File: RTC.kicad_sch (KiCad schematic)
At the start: 14 parts, among them J17 Molex 470531000, U11 EMC2301-1-ACZL-TR, U14 74LVC1G07SE-7, U8 PCF85063AT/AAZ, Y2 X32K768S301

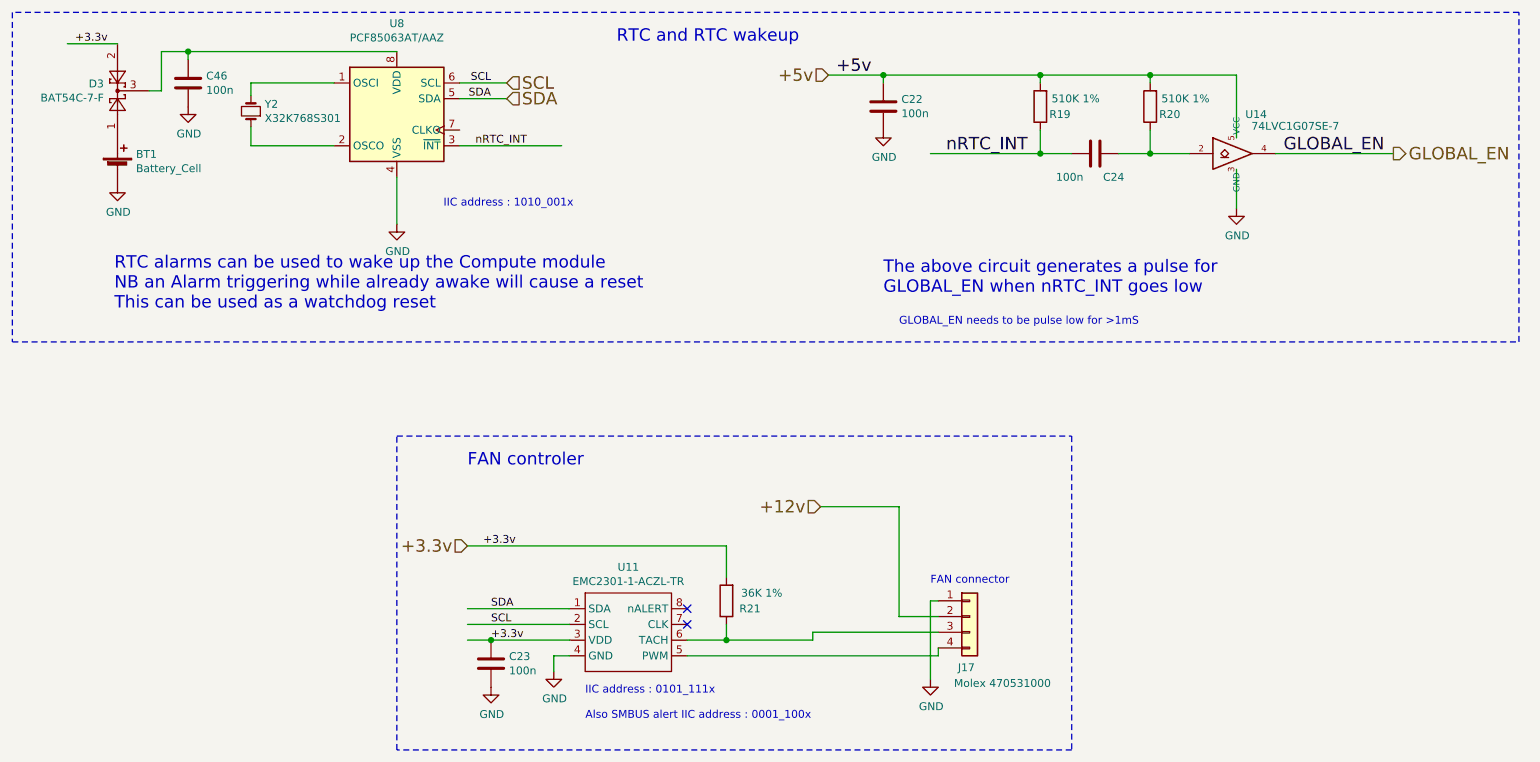
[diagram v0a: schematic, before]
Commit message: Removing unneeded items
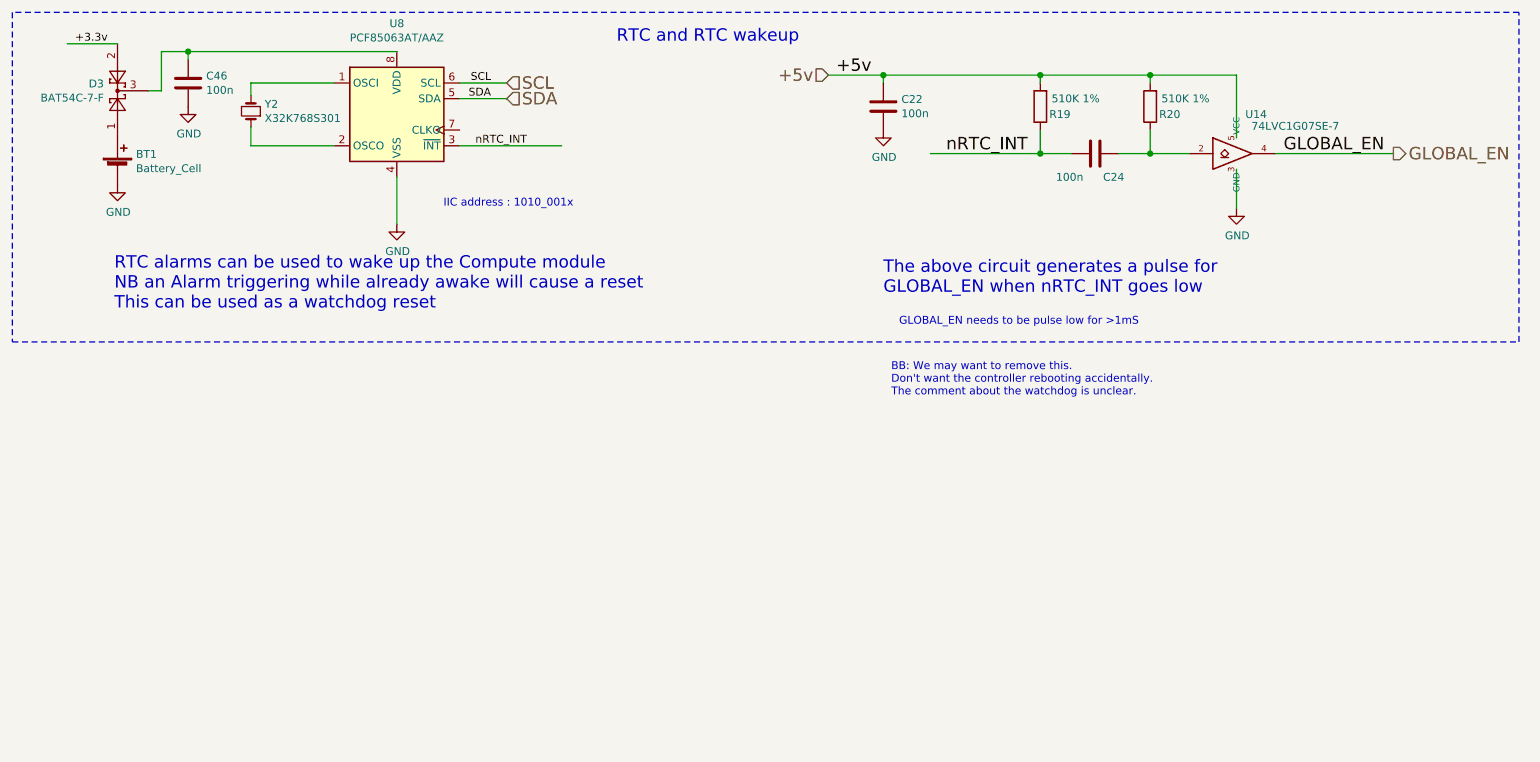
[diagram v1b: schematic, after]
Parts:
- removed C23: 100n, Capacitor_SMD:C_0402_1005Metric, symbol Device:C
- removed J17: Molex 470531000, Connector:FanPinHeader_1x04_P2.54mm_Vertical, symbol Connector_Generic:Conn_01x04
- removed R21: 36K 1%, Resistor_SMD:R_0402_1005Metric, symbol Device:R
- removed U11: EMC2301-1-ACZL-TR, Package_SO:MSOP-8_3x3mm_P0.65mm, symbol CM4IO:EMC2301
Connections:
- no-connect marks 2 -> 0
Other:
- note added: "BB: We may want to remove this. Don't want the controller rebooting accidentally. The comment about the watchdog is unclear."
- note removed: "Also SMBUS alert IIC address : 0001_100x"
- note removed: "FAN connector"
- note removed: "FAN controler"
- note removed: "IIC address : 0101_111x"
